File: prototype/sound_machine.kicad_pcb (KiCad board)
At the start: 2 copper layers, 75 x 45 mm, 21 parts, among them J1 Conn_01x04, J10 Conn_01x01, J11 Conn_01x01, J12 Conn_01x01, J13 Conn_01x15, J16 Conn_01x15, J2 Conn_01x15, J3 Conn_01x15, J4 Conn_01x08, J5 Audio-Jack-3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

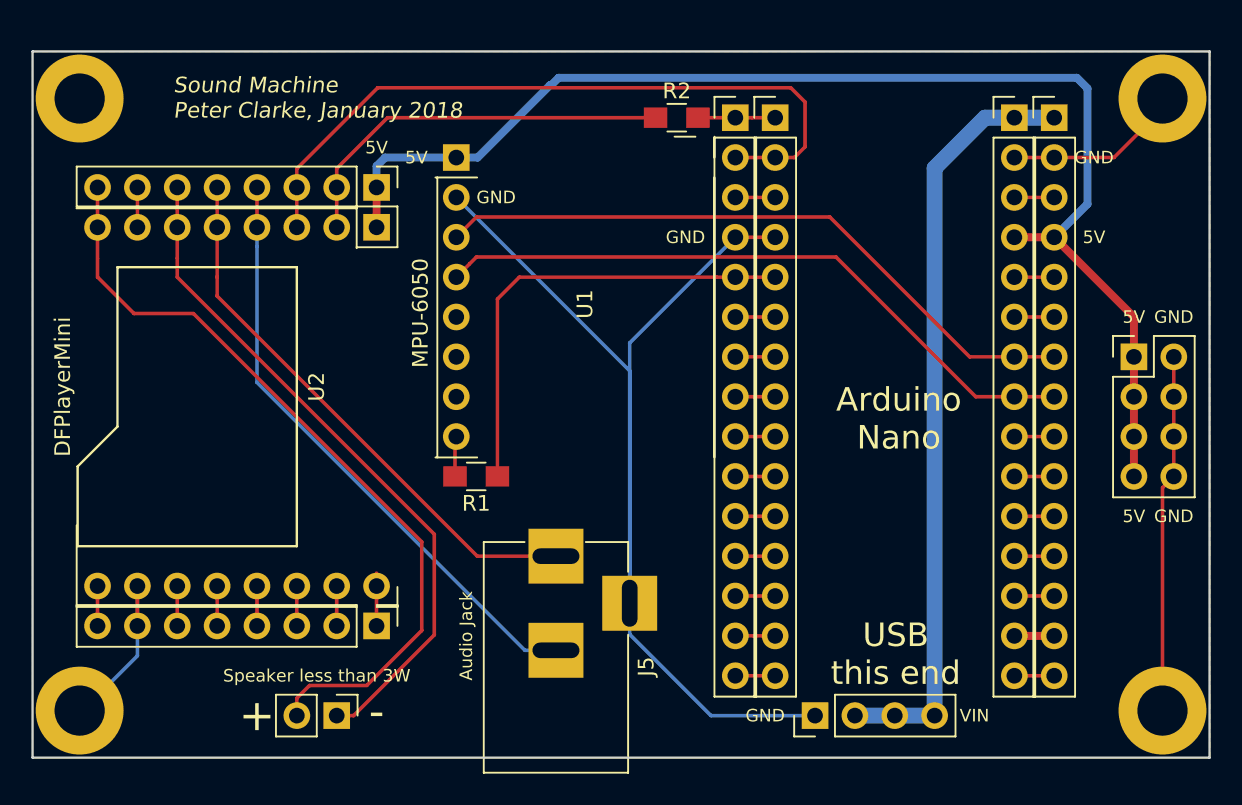
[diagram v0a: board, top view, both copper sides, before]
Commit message: Removed jack
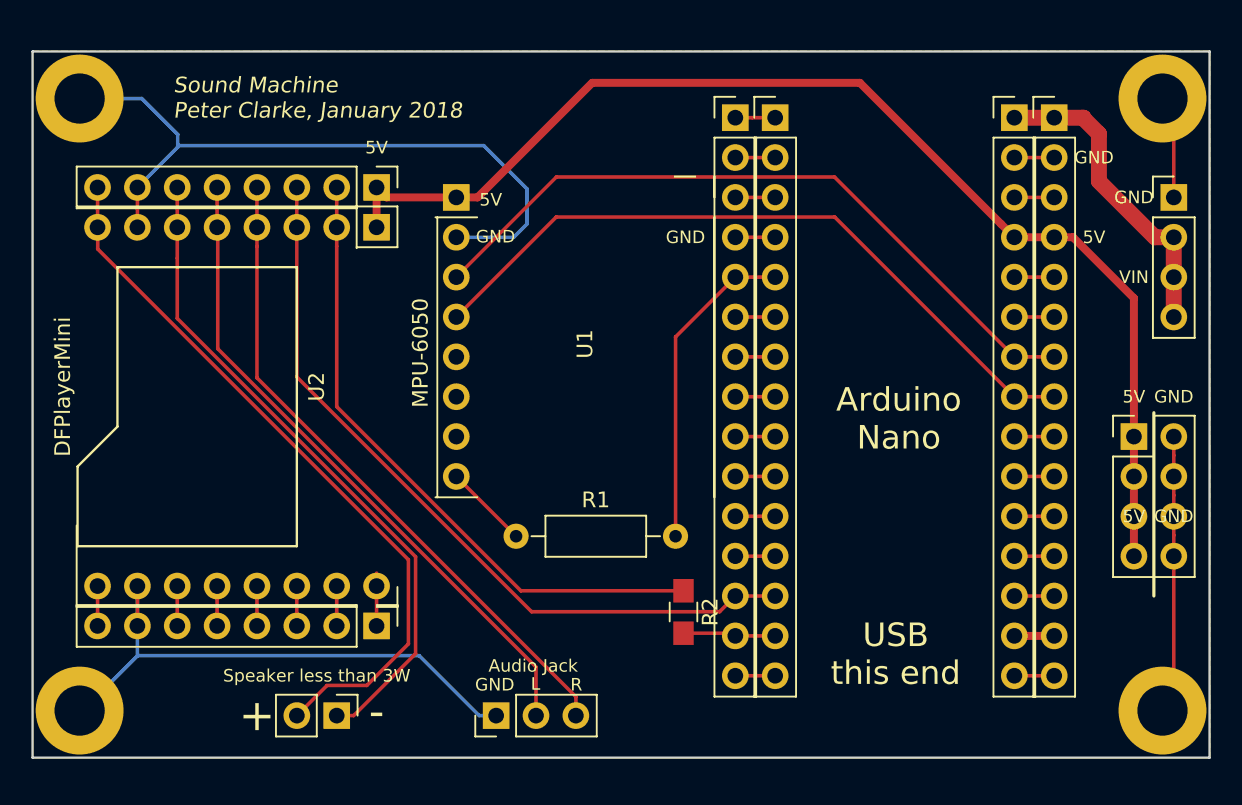
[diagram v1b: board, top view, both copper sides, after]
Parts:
- J5: value Audio-Jack-3 -> Conn_01x03; footprint Connectors:BARREL_JACK -> Pin_Headers:Pin_Header_Straight_1x03_Pitch2.54mm
- R1: footprint Resistors_SMD:R_0805_HandSoldering -> Resistors_THT:R_Axial_DIN0207_L6.3mm_D2.5mm_P10.16mm_Horizontal
- moved J1 40.2 mm to (172.7, 114.3), turned to 0 degrees
- moved R2 31.5 mm to (141.5, 140.7), turned to 270 degrees
- moved REF** 23.4 mm to (103.6, 132.1)
- moved J5 10.9 mm to (129.5, 147.3)
- moved J7 5.08 mm to (170.2, 129.5)
- moved R1 4.58 mm to (130.8, 135.9)
- moved U1 2.54 mm to (127.0, 114.3)
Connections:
- J4 pad 3: RX0 -> D10
- J4 pad 4: Net-(J4-Pad4) -> /DAC_R
- J4 pad 5: Net-(J4-Pad5) -> /DAC_L
- J5 pad 1: Net-(J4-Pad5) -> GND
- J5 pad 2: Net-(J4-Pad4) -> /DAC_L
- J5 pad 3: GND -> /DAC_R
- R2 pad 2: TX1 -> D11
- U2 pad 3: RX0 -> D10
- U2 pad 4: Net-(J4-Pad4) -> /DAC_R
- U2 pad 5: Net-(J4-Pad5) -> /DAC_L
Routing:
- net D10: track 2.54 -> 49.2 mm
- net RX0: track 46.2 -> 2.54 mm
- net /DAC_L: track 0.00 -> 42.5 mm
- net /DAC_R: track 0.00 -> 42.1 mm
- net Net-(J4-Pad4): track 38.6 -> 0.00 mm
- net Net-(J4-Pad5): track 35.1 -> 0.00 mm
- net VIN: track 48.9 -> 20.2 mm
- net Net-(J4-Pad2): track 26.6 -> 42.1 mm
- net GND: track 121.6 -> 109.9 mm
- net D2: track 29.6 -> 20.6 mm
- net +5V: track 82.1 -> 76.2 mm
- net Net-(J4-Pad8): track 49.2 -> 45.7 mm
- net D11: track 2.54 -> 5.91 mm
- net SDA: track 42.3 -> 45.5 mm
- net SCL: track 42.3 -> 45.5 mm
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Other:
- board text added: "L"
- board text added: "R"

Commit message: Rounded corners
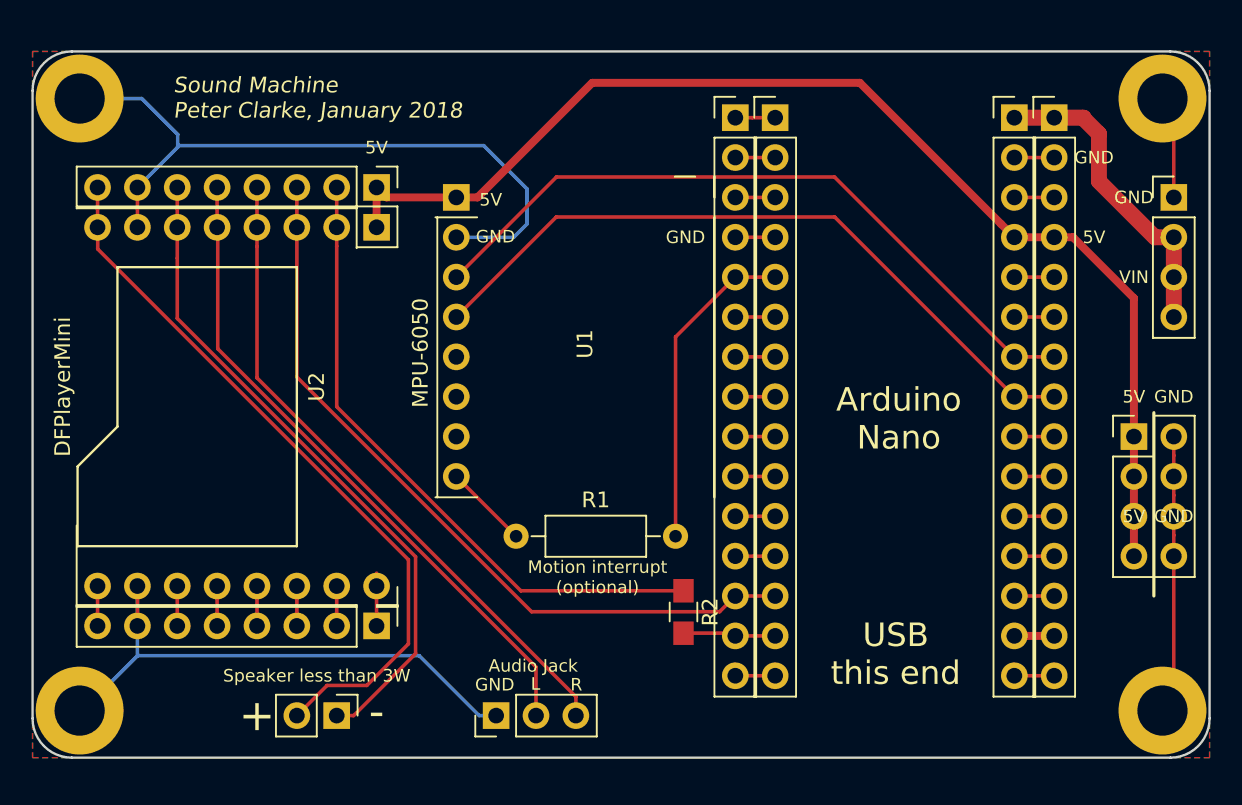
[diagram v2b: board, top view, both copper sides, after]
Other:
- outline, holes or cut-outs redrawn
- board text added: "Motion interrupt (optional)"
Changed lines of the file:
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@@
     (area 99.924999 104.924999 175.075001 150.075001)
     (thickness 1.6)
-    (drawings 53)
+    (drawings 58)
     (tracks 156)
     (zones 0)
@@
     (uvia_drill 0.1)
     (add_net VIN)
+  )
+  (module Mounting_Holes:MountingHole_3.2mm_M3_DIN965_Pad (layer F.Cu)
+    (at 103 108)
+    (descr "Mounting Hole 3.2mm, M3, DIN965")
+    (tags "mounting hole 3.2mm m3 din965")
+    (fp_text reference J12 (at 0 -3.8) (layer F.Fab)
+      (effects (font (size 1 1) (thickness 0.15)))
+    )
+    (fp_text value Conn_01x01 (at 0 3.8) (layer F.Fab)
+      (effects (font (size 1 1) (thickness 0.15)))
+    )
+    (fp_circle (center 0 0) (end 2.8 0) (layer Cmts.User) (width 0.15))
+    (fp_circle (center 0 0) (end 3.05 0) (layer F.CrtYd) (width 0.05))
+    (pad 1 thru_hole circle (at 0 0) (size 5.6 5.6) (drill 3.2) (layers *.Cu *.Mask)
+      (net 2 GND))
   )
   (module sound_machine:MPU-6050 placed (layer F.Cu)
@@
       (net 2 GND))
   )
-  (module Mounting_Holes:MountingHole_3.2mm_M3_DIN965_Pad (layer F.Cu)
-    (at 103 108)
-    (descr "Mounting Hole 3.2mm, M3, DIN965")
-    (tags "mounting hole 3.2mm m3 din965")
-    (fp_text reference J12 (at 0 -3.8) (layer F.Fab)
-      (effects (font (size 1 1) (thickness 0.15)))
-    )
-    (fp_text value Conn_01x01 (at 0 3.8) (layer F.Fab)
-      (effects (font (size 1 1) (thickness 0.15)))
-    )
-    (fp_circle (center 0 0) (end 2.8 0) (layer Cmts.User) (width 0.15))
-    (fp_circle (center 0 0) (end 3.05 0) (layer F.CrtYd) (width 0.05))
-    (pad 1 thru_hole circle (at 0 0) (size 5.6 5.6) (drill 3.2) (layers *.Cu *.Mask)
-      (net 2 GND))
-  )
   (module theapi:TheApiLogoTiny (layer F.Cu)
     (at 107.442 105.156)
@@
     )
   )
+  (gr_line (start 172.5 150) (end 102.5 150) (angle 90) (layer Edge.Cuts) (width 0.15))
+  (gr_line (start 175 107.5) (end 175 147.5) (angle 90) (layer Edge.Cuts) (width 0.15))
+  (gr_line (start 102.5 105) (end 172.5 105) (angle 90) (layer Edge.Cuts) (width 0.15))
+  (gr_line (start 100 147.5) (end 100 107.5) (angle 90) (layer Edge.Cuts) (width 0.15))
+  (gr_arc (start 102.5 147.5) (end 102.5 150) (angle 90) (layer Edge.Cuts) (width 0.15))
+  (gr_arc (start 172.5 147.5) (end 175 147.5) (angle 90) (layer Edge.Cuts) (width 0.15))
+  (gr_arc (start 172.5 107.5) (end 172.5 105) (angle 90) (layer Edge.Cuts) (width 0.15))
+  (gr_arc (start 102.5 107.5) (end 100 107.5) (angle 90) (layer Edge.Cuts) (width 0.15))
+  (gr_text "Motion interrupt \n(optional)" (at 136 138.5) (layer F.SilkS)
+    (effects (font (size 0.8 0.8) (thickness 0.1)))
+  )
   (gr_text GND (at 129.5 116.8) (layer B.SilkS)
     (effects (font (size 0.8 0.8) (thickness 0.1)) (justify mirror))
@@
     (arrow2b (pts (xy 85 150) (xy 84.413579 148.873496)))
   )
-  (gr_line (start 175 105) (end 175 150) (angle 90) (layer Edge.Cuts) (width 0.15))
-  (gr_line (start 100 105) (end 175 105) (angle 90) (layer Edge.Cuts) (width 0.15))
-  (gr_line (start 100 150) (end 100 105) (angle 90) (layer Edge.Cuts) (width 0.15))
-  (gr_line (start 175 150) (end 100 150) (angle 90) (layer Edge.Cuts) (width 0.15))
   (dimension 75 (width 0.3) (layer Cmts.User)
     (gr_text "75.000 mm" (at 137.5 161.35) (layer Cmts.User)

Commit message: Capacitor
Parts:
- added C1: 10uf, Capacitors_THT:CP_Radial_D5.0mm_P2.50mm, F.Cu at (170.2, 128.3)
- J1: footprint Pin_Headers:Pin_Header_Straight_1x04_Pitch2.54mm -> Socket_Strips:Socket_Strip_Straight_1x04
- J13, J16: footprint Pin_Headers:Pin_Header_Straight_1x15_Pitch2.54mm -> Socket_Strips:Socket_Strip_Straight_1x15_Pitch2.54mm
- U1: footprint sound_machine:MPU-6050 -> MPU-6050
- moved J7 5.08 mm to (170.2, 134.6)
- moved U1 1.02 mm to (126.0, 114.3)
- turned J1 to 270 degrees
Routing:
- net +5V: track 76.2 -> 82.2 mm
- net Net-(R1-Pad1): track 5.39 -> 6.40 mm
- net SDA: track 45.5 -> 46.5 mm
- net SCL: track 45.5 -> 46.5 mm
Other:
- board text added: "https://github.com/theapi/sound_machine_hardware prototype v1.1.0"
- board text removed: "https://github.com/theapi/sound_machine_hardware prototype v1.0.0"

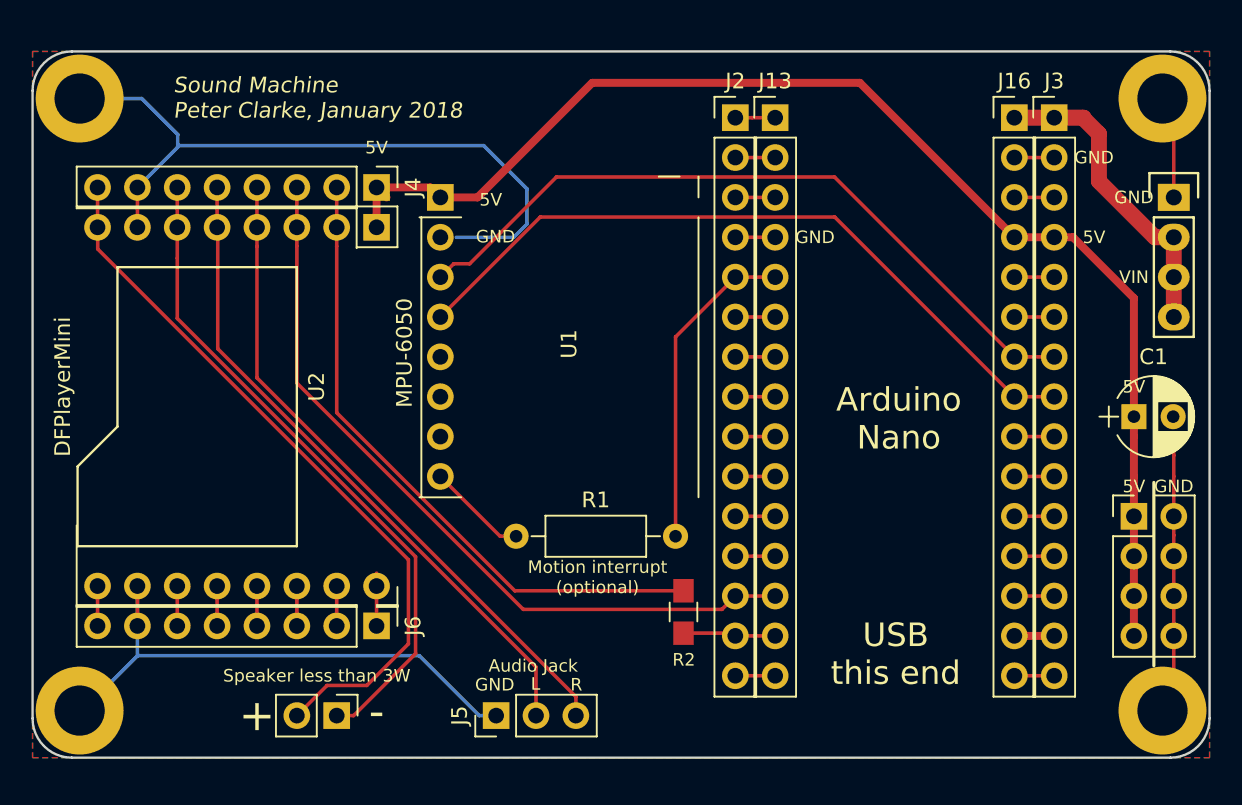
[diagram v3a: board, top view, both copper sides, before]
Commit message: Layout change
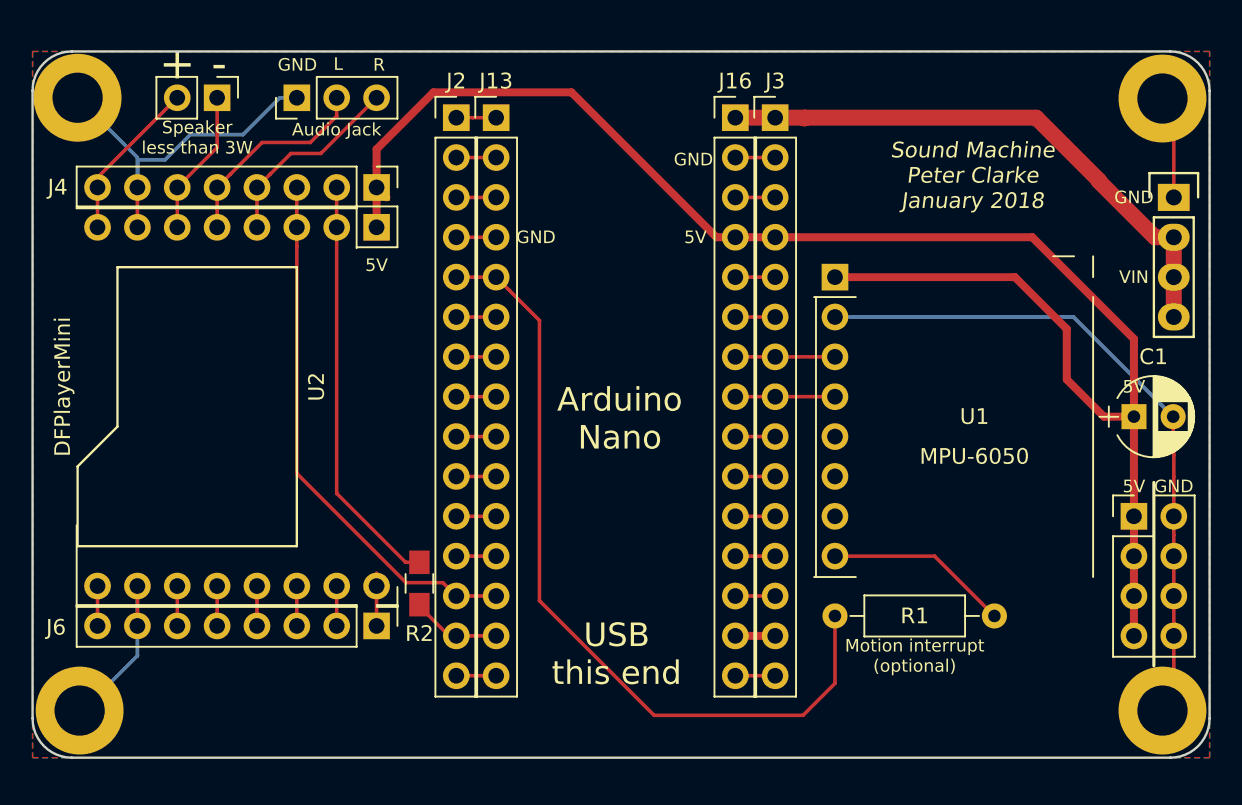
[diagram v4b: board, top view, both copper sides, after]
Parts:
- removed the REF** at (155.7, 112.8)
- moved REF** 46.5 mm to (153.6, 110.8)
- moved J5 41.4 mm to (116.8, 108.0)
- moved LS1 40.1 mm to (111.8, 108.0)
- moved R1 30.9 mm to (161.3, 141.0), turned to 180 degrees
- moved U1 25.7 mm to (151.1, 119.4)
- moved J13 17.8 mm to (129.5, 109.2)
- moved J16 17.8 mm to (144.8, 109.2)
- moved J2 17.8 mm to (127.0, 109.2)
- moved J3 17.8 mm to (147.3, 109.2)
- moved REF** 16.9 mm to (118.7, 124.3)
- moved R2 16.9 mm to (124.7, 138.9)
- moved J12 0.14 mm to (102.9, 108.0)
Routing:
- net SCL: track 46.5 -> 6.35 mm
- net SDA: track 46.5 -> 6.35 mm
- net Net-(J4-Pad8): track 45.7 -> 10.4 mm
- net Net-(J4-Pad6): track 42.0 -> 9.31 mm
- net D2: track 20.6 -> 51.3 mm
- net /DAC_R: track 42.1 -> 12.5 mm
- net /DAC_L: track 42.5 -> 13.6 mm
- net +5V: track 82.2 -> 105.7 mm
- net GND: track 109.9 -> 89.8 mm
- net VIN: track 20.2 -> 36.3 mm
- net D10: track 49.3 -> 34.2 mm
- net Net-(J4-Pad2): track 42.4 -> 27.8 mm
- net Net-(R1-Pad1): track 6.40 -> 11.7 mm
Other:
- board text added: "Sound Machine Peter Clarke January 2018"
- board text removed: "Sound Machine Peter Clarke, January 2018"
